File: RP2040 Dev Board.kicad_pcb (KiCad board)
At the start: 4 copper layers, 20.3 x 48.3 mm, 101 parts, among them J101 Conn_01x19, J102 Conn_01x19, J103 Conn_01x03, J201 TYPE-C-31-M-12, SW202 ~{USB_BOOT}, U201 AZ1117R-3.3TRE1, U202 RP2040, U205 W25Q128JVS, Y201 Crystal_GND24

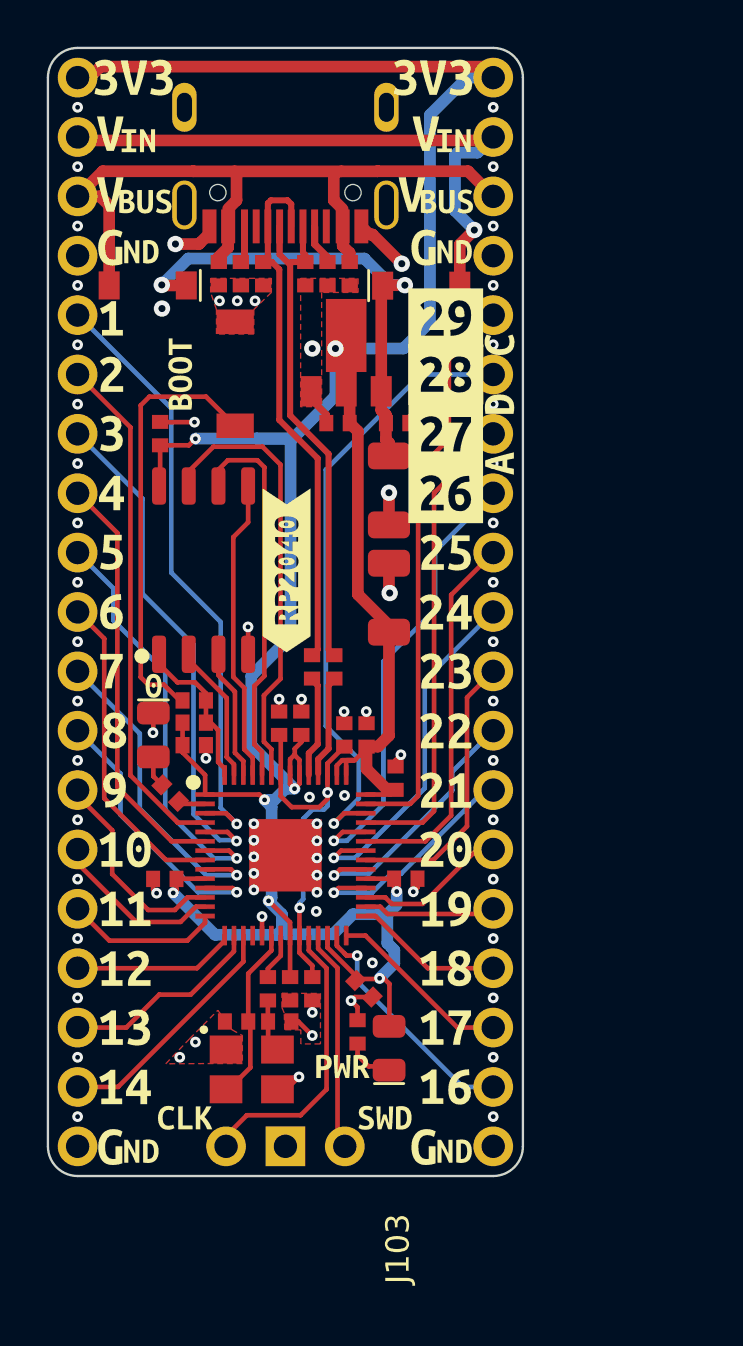
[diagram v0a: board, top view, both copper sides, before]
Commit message: Rev 2
Ready to order Rev2:
-Routed missing 1.1V rail
-Swapped LED footprints from 0603 to 0805
-Pins 43 &44 routed to nearest decoupling cap
-Crystal replaced with basic part and created 3D model
-ADC silkscreen improved
-Minor Silkscreen changes
-Generated new gerbers, renders, and PDFs
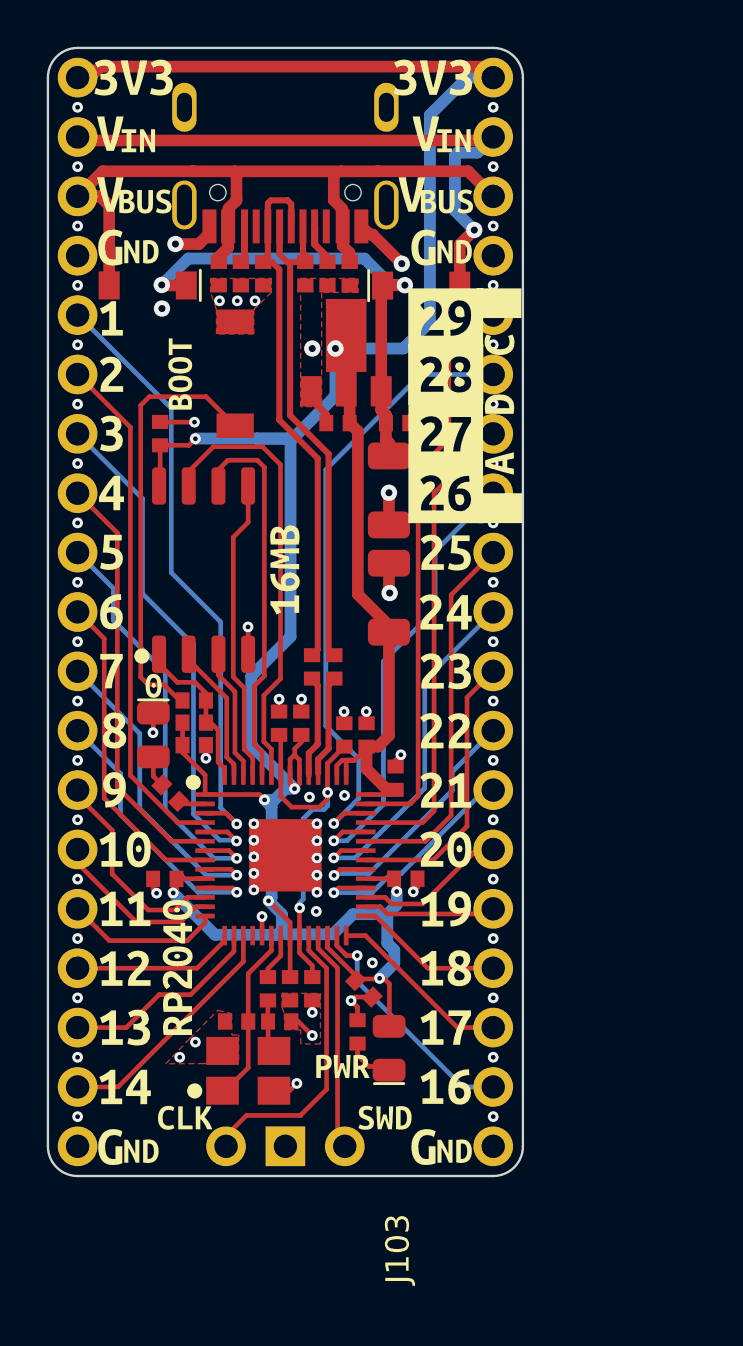
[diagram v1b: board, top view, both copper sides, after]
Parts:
- removed kibuzzard-624CF1B9: G***, kibuzzard-624CF1B9
- removed kibuzzard-624CF22E: G***, kibuzzard-624CF22E
- removed kibuzzard-624D057F: G***, kibuzzard-624D057F
- added kibuzzard-62659E4E: G***, kibuzzard-62659E4E, B.Cu at (153.1, 53.7)
- added kibuzzard-62659F2B: G***, kibuzzard-62659F2B, B.Cu at (147.0, 36.1)
- added kibuzzard-6265A18F: G***, kibuzzard-6265A18F, F.Cu at (142.3, 66.1)
- added kibuzzard-6265A1A8: G***, kibuzzard-6265A1A8, F.Cu at (146.9, 49.1)
- added kibuzzard-6265A538: G***, kibuzzard-6265A538, B.Cu at (150.2, 42.4)
- Y201: footprint Breadstick Footprints:7V12000018 -> X322516MLB4SI:OSC_X322516MLB4SI
- moved Y201 0.16 mm to (145.3, 70.5), turned to 90 degrees

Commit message: Rev 3
JLCPCB noticed a mistake in my order, I had remnants from an early version in the gerbers folder. Cleared that out and made some updates to the board and resubmitted as Rev3. I added a GND via that was missing near a 3.3V via underneath the RP2040, added Rev 3 to the silkscreen, and nudged C207 away from the USB lines and added a GND via. Gerbers, drill, and centroid files regenerated. Rev 3 renders generated as well.
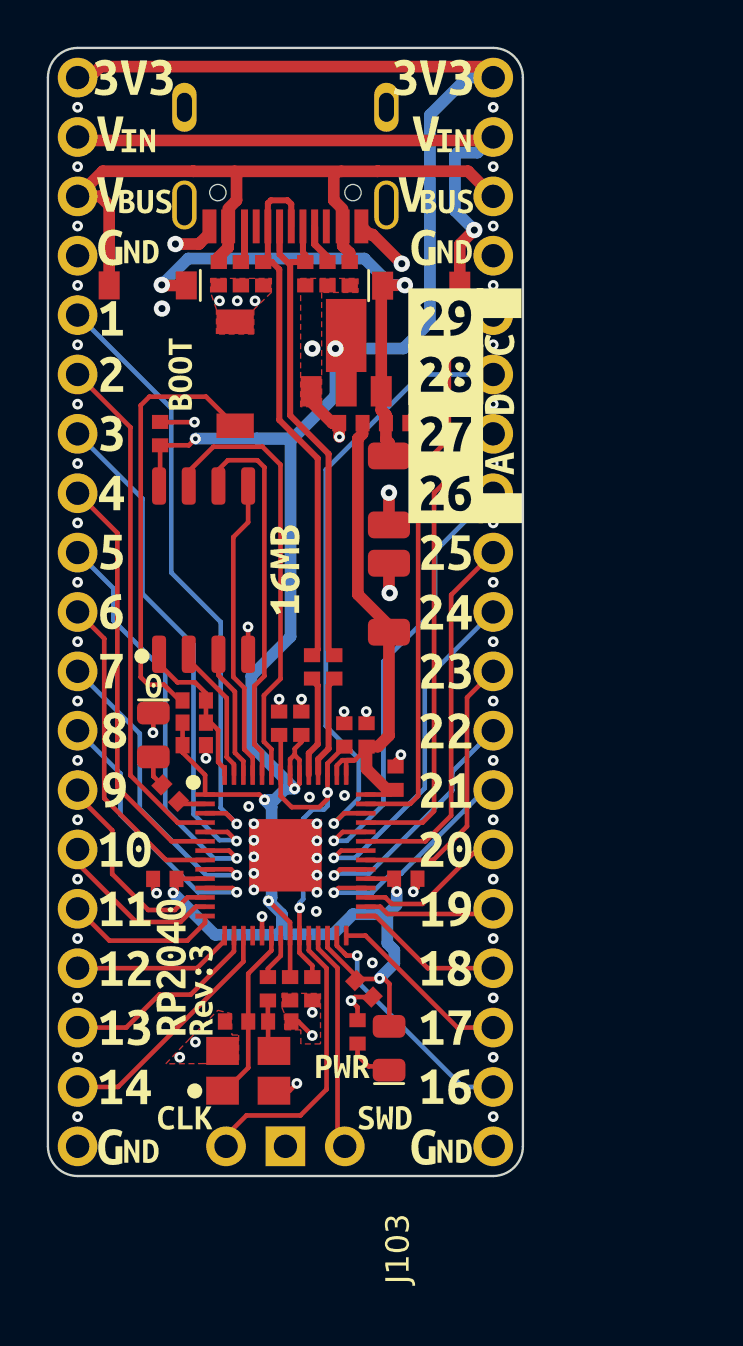
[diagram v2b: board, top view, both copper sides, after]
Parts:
- added kibuzzard-6267242B: G***, kibuzzard-6267242B, F.Cu at (143.3, 67.1)
- moved C207 0.55 mm to (149.7, 42.8)
- moved kibuzzard-6265A18F 0.28 mm to (142.0, 66.1)
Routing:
- net GND: track 23.6 -> 25.3 mm, vias 78 -> 80
- net 3V3_LDO: track 134.2 -> 132.6 mm

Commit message: Made changes to schematic and PCB
Swapped pin 0 and pin 14.
Added missing trace from regulator to capacitors.
Widened power distribution traces.
Aligned LEDs.
Adjusted Silkscreen.
Updated Revision number to 4
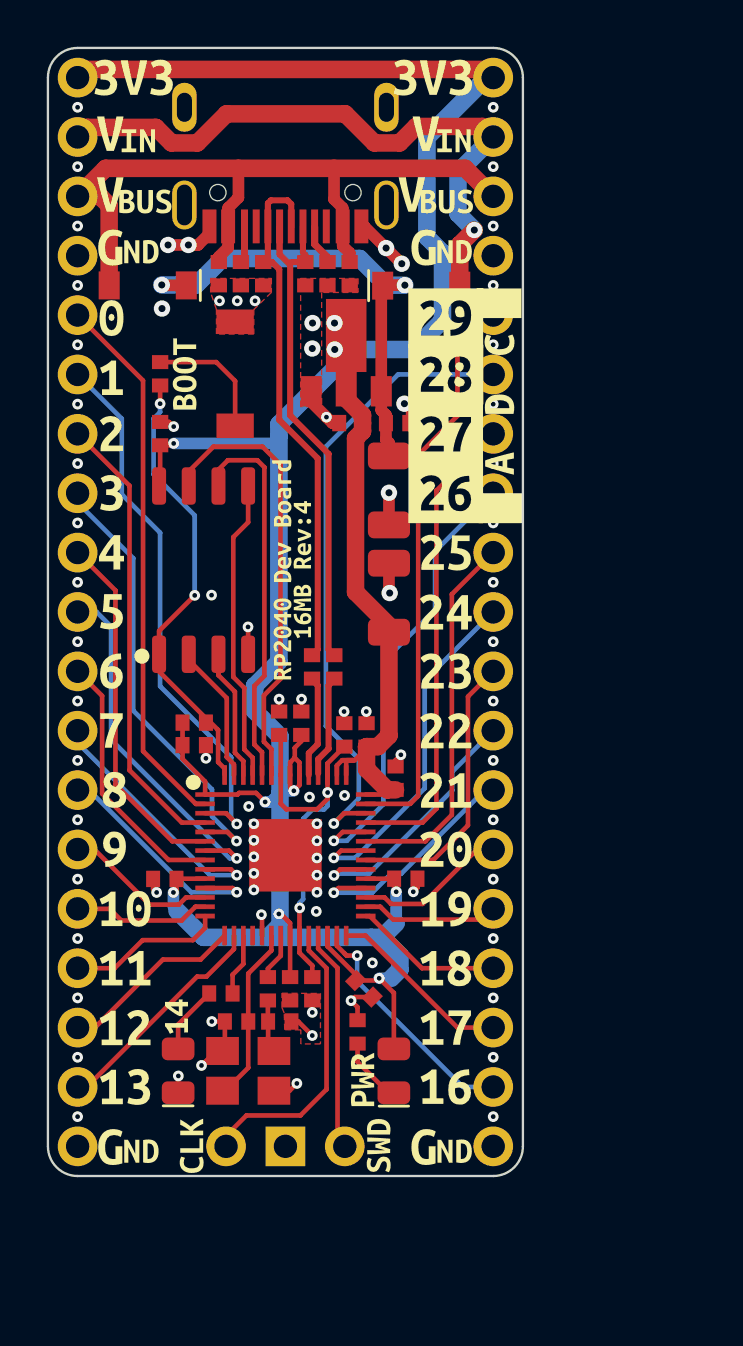
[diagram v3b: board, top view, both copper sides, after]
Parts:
- removed kibuzzard-624A356E: G***, kibuzzard-624A356E
- removed kibuzzard-624A389A: G***, kibuzzard-624A389A
- removed kibuzzard-6265A18F: G***, kibuzzard-6265A18F
- removed kibuzzard-6265A1A8: G***, kibuzzard-6265A1A8
- removed kibuzzard-6267242B: G***, kibuzzard-6267242B
- added kibuzzard-62830DE2: G***, kibuzzard-62830DE2, F.Cu at (139.5, 38.3)
- added kibuzzard-62830E7F: G***, kibuzzard-62830E7F, F.Cu at (142.2, 68.2)
- added kibuzzard-62831E36: G***, kibuzzard-62831E36, F.Cu at (146.8, 49.1)
- added kibuzzard-62831F6A: G***, kibuzzard-62831F6A, F.Cu at (147.6, 49.1)
- moved D101 14.4 mm to (142.3, 70.5), turned to 90 degrees
- moved R211 14.1 mm to (141.6, 40.7), turned to 180 degrees
- moved R102 8.84 mm to (144.2, 67.2), turned to -90 degrees
- moved kibuzzard-6265A538 8.41 mm to (146.7, 34.7)
- moved kibuzzard-62659F2B 6.28 mm to (140.7, 35.4)
- moved kibuzzard-62659E4E 5.91 mm to (153.1, 47.8)
- moved kibuzzard-624A34FB 2.54 mm to (139.5, 48.3)
- moved kibuzzard-624A3549 2.54 mm to (140.1, 63.6)
- moved kibuzzard-624A355B 2.54 mm to (140.1, 68.7)
- moved kibuzzard-624A34DF 2.54 mm to (139.5, 40.9)
- moved kibuzzard-624A34EB 2.54 mm to (139.5, 43.3)
- moved kibuzzard-624A34F5 2.54 mm to (139.5, 45.8)
- moved kibuzzard-624A3524 2.54 mm to (139.5, 50.9)
- moved kibuzzard-624A352B 2.54 mm to (139.5, 53.4)
- moved kibuzzard-624A3534 2.54 mm to (139.5, 56.0)
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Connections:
- J101 pad 10: GPIO6 -> GPIO5
- J101 pad 11: GPIO7 -> GPIO6
- J101 pad 12: GPIO8 -> GPIO7
- J101 pad 13: GPIO9 -> GPIO8
- J101 pad 14: GPIO10 -> GPIO9
- J101 pad 15: GPIO11 -> GPIO10
- J101 pad 16: GPIO12 -> GPIO11
- J101 pad 17: GPIO13 -> GPIO12
- J101 pad 18: GPIO14 -> GPIO13
- J101 pad 5: GPIO1 -> GPIO0
- J101 pad 6: GPIO2 -> GPIO1
- J101 pad 7: GPIO3 -> GPIO2
- J101 pad 8: GPIO4 -> GPIO3
- J101 pad 9: GPIO5 -> GPIO4
- R102 pad 2: GPIO0 -> GPIO14
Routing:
- net GPIO0: track 1.19 -> 23.4 mm
- net Net-(R211-Pad1): track 18.5 -> 5.46 mm
- net /RP2040/MCU_QSPI_CSN: track 6.89 -> 19.4 mm, vias 0 -> 2
- net GPIO14: track 10.4 -> 2.67 mm
- net 3V3_LDO: track 132.6 -> 137.1 mm, vias 8 -> 9
- net GPIO3: track 22.1 -> 19.2 mm
- net GPIO2: track 22.1 -> 19.5 mm
- net GPIO7: track 13.8 -> 11.1 mm
- net GPIO6: track 13.9 -> 11.2 mm
- net GPIO4: track 18.0 -> 15.4 mm
- net GPIO1: track 26.1 -> 23.6 mm
- net GPIO9: track 9.04 -> 6.56 mm
- net GPIO5: track 18.0 -> 15.5 mm
- net GPIO8: track 12.1 -> 10.0 mm
- net GND: track 25.3 -> 27.2 mm, vias 80 -> 84
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
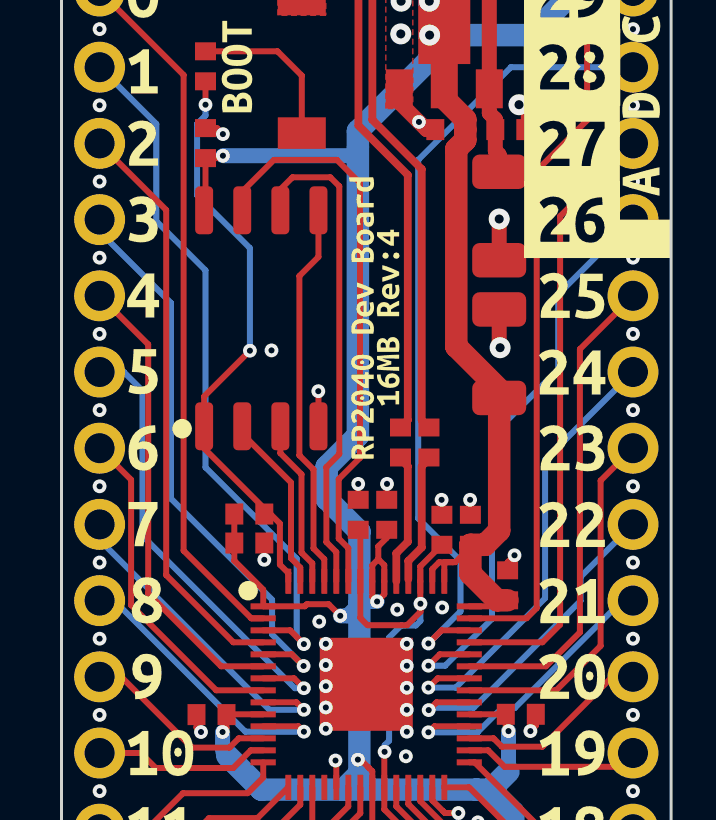
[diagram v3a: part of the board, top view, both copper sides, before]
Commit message: Increased separation between QSPI bus lines
Now that the LED is no longer connected to pin 0, there was room to make adjustments that allowed for better separation between the QSPI bus lines.
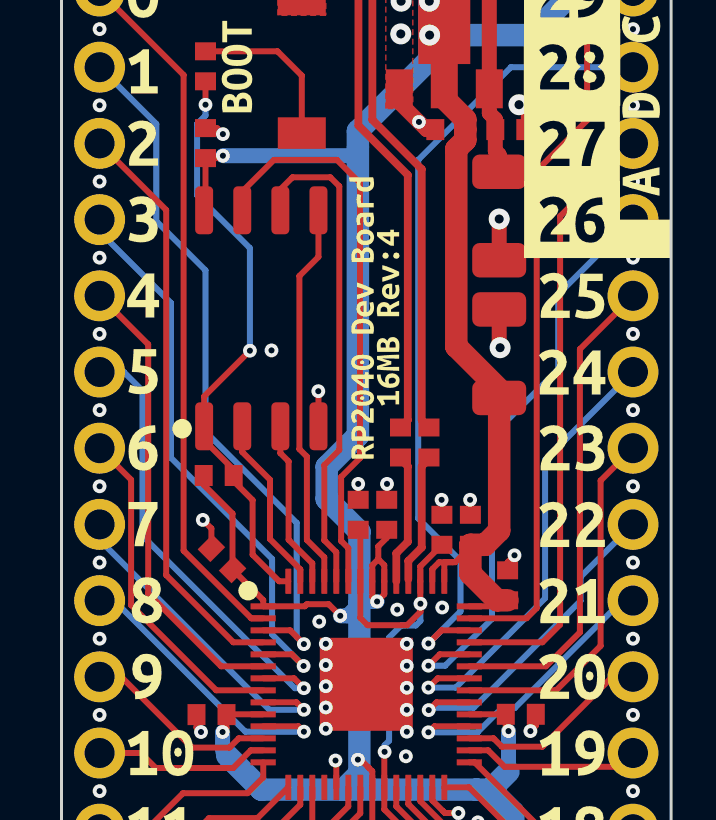
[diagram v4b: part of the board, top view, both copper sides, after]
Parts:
- moved R213 1.64 mm to (142.0, 54.3)
- moved C212 1.05 mm to (142.1, 57.1), turned to 45 degrees
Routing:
- net 3V3_LDO: track 137.1 -> 138.8 mm
- net GND: track 27.2 -> 27.7 mm

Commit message: Removed unconnected traces found by DRC
During the last edit, some very short traces that didn't extend beyond the pad they were connected to were overlooked. They've now been deleted and the DRC is coming back clean.
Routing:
- net /RP2040/MCU_QSPI_CSN: track 19.5 -> 19.0 mm
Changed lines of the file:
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@@
   (segment (start 142.49 54.15) (end 141.505 53.165) (width 0.2) (layer "F.Cu") (net 16))
   (segment (start 143.12 56.98) (end 143.12 55.16) (width 0.2) (layer "F.Cu") (net 16))
-  (segment (start 141.505 53.165) (end 141.505 52.7) (width 0.2) (layer "F.Cu") (net 16))
   (segment (start 144.005 57.865) (end 143.12 56.98) (width 0.2) (layer "F.Cu") (net 16))
   (segment (start 143.12 55.16) (end 142.49 54.53) (width 0.2) (layer "F.Cu") (net 16))
@@
   (segment (start 142.49 54.34) (end 142.49 54.15) (width 0.2) (layer "F.Cu") (net 16))
   (segment (start 144.31 57.865) (end 144.005 57.865) (width 0.2) (layer "F.Cu") (net 16))
-  (segment (start 141.55 52.745) (end 141.505 52.7) (width 0.2) (layer "F.Cu") (net 16))
   (segment (start 141.505 51.705) (end 143.03 50.18) (width 0.2) (layer "F.Cu") (net 16))
   (via (at 141.55 41.98) (size 0.46) (drill 0.2) (layers "F.Cu" "B.Cu") (net 16))

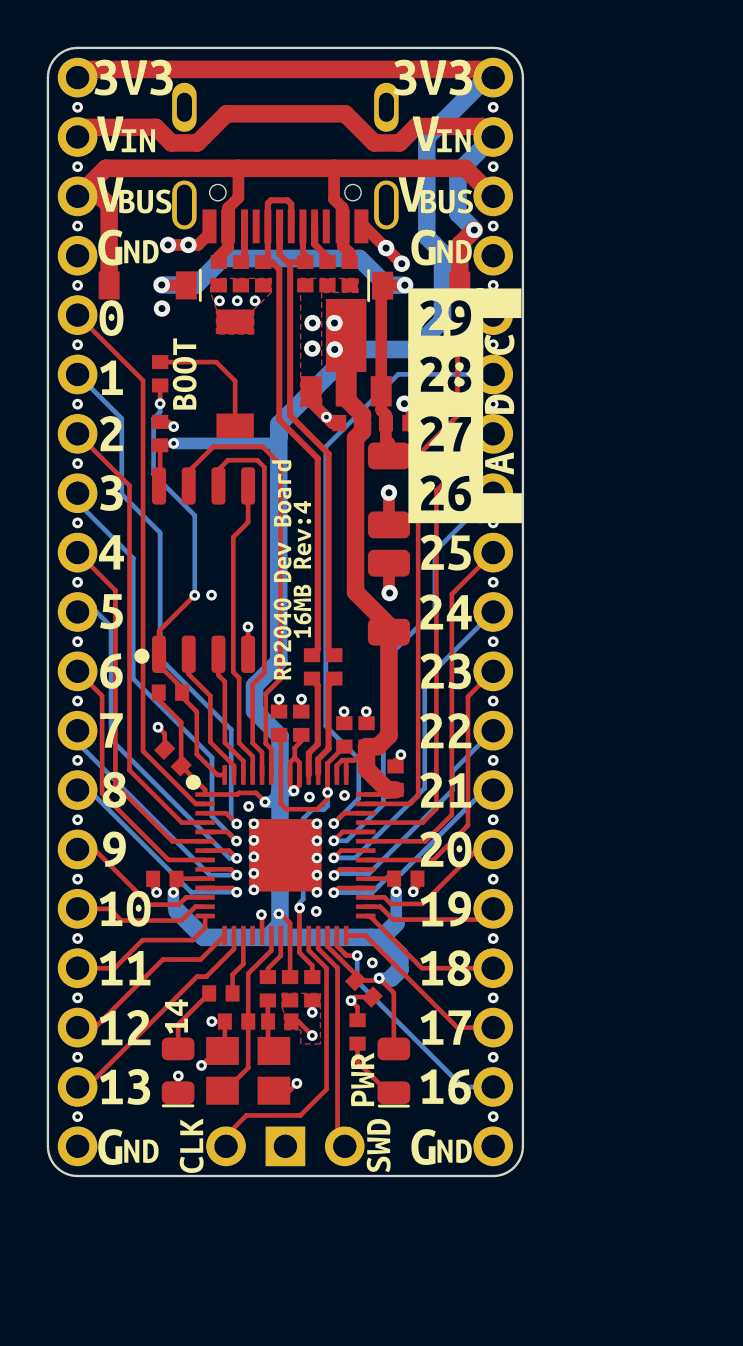
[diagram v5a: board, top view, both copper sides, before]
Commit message: Modified Silkscreen and Added Renders
Added OSHW logo and made other silkscreen changes.
Generated a render of the front of the board.
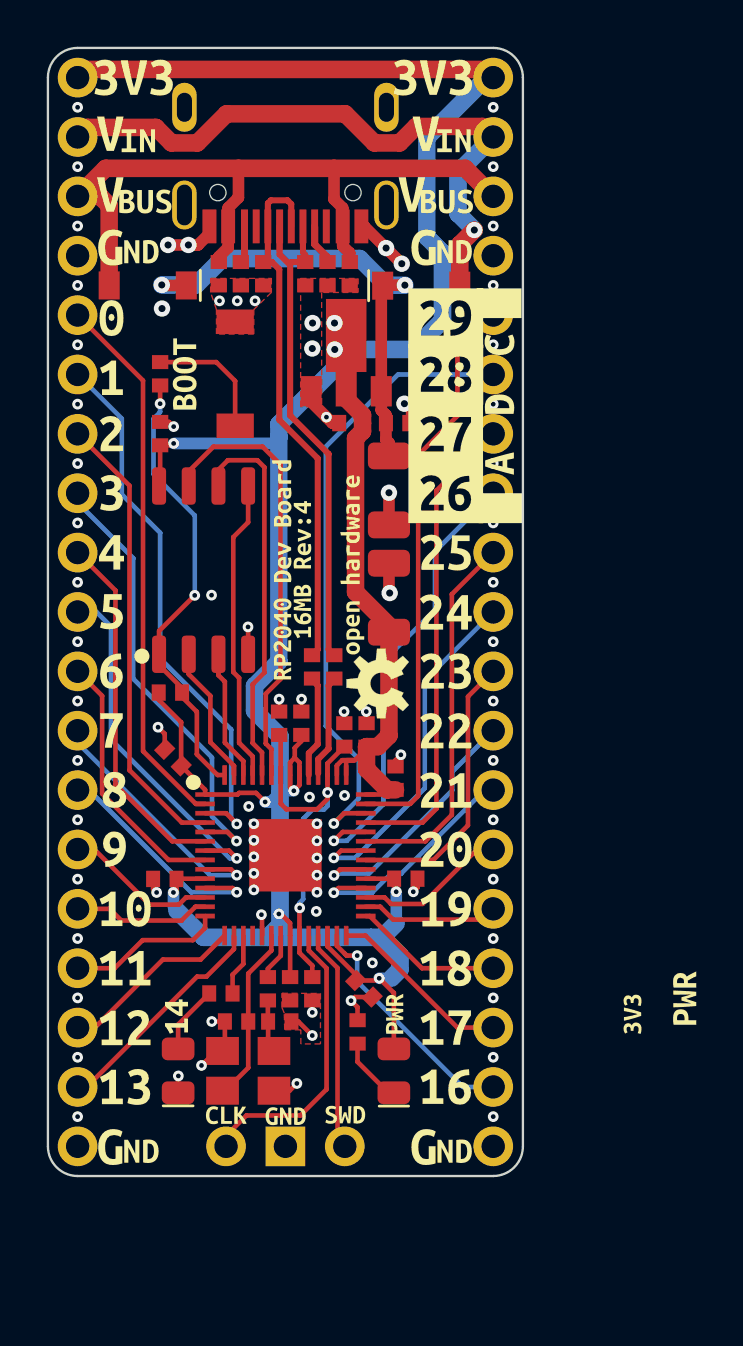
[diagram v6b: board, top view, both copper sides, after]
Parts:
- removed kibuzzard-624A37B5: G***, kibuzzard-624A37B5
- removed kibuzzard-624A37C8: G***, kibuzzard-624A37C8
- added ?: , Aesthetics:OSHW-LOGO-S, F.Cu at (151.0, 54.0)
- added kibuzzard-6283F25A: G***, kibuzzard-6283F25A, F.Cu at (149.8, 48.9)
- added kibuzzard-6283F3A6: G***, kibuzzard-6283F3A6, F.Cu at (161.8, 68.1)
- added kibuzzard-6283F3DA: G***, kibuzzard-6283F3DA, F.Cu at (144.4, 72.4)
- added kibuzzard-6283F3E3: G***, kibuzzard-6283F3E3, F.Cu at (146.9, 72.5)
- added kibuzzard-6283F3EB: G***, kibuzzard-6283F3EB, F.Cu at (149.5, 72.4)
- added kibuzzard-6283F49B: G***, kibuzzard-6283F49B, F.Cu at (151.6, 68.1)
- moved kibuzzard-624A3833 14.2 mm to (164.0, 67.4)
